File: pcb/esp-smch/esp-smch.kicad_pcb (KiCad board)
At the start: 2 copper layers, 54.7 x 41.5 mm, 7 parts, among them U1 WeMos_D1_mini, U2 NRF24L01_Breakout

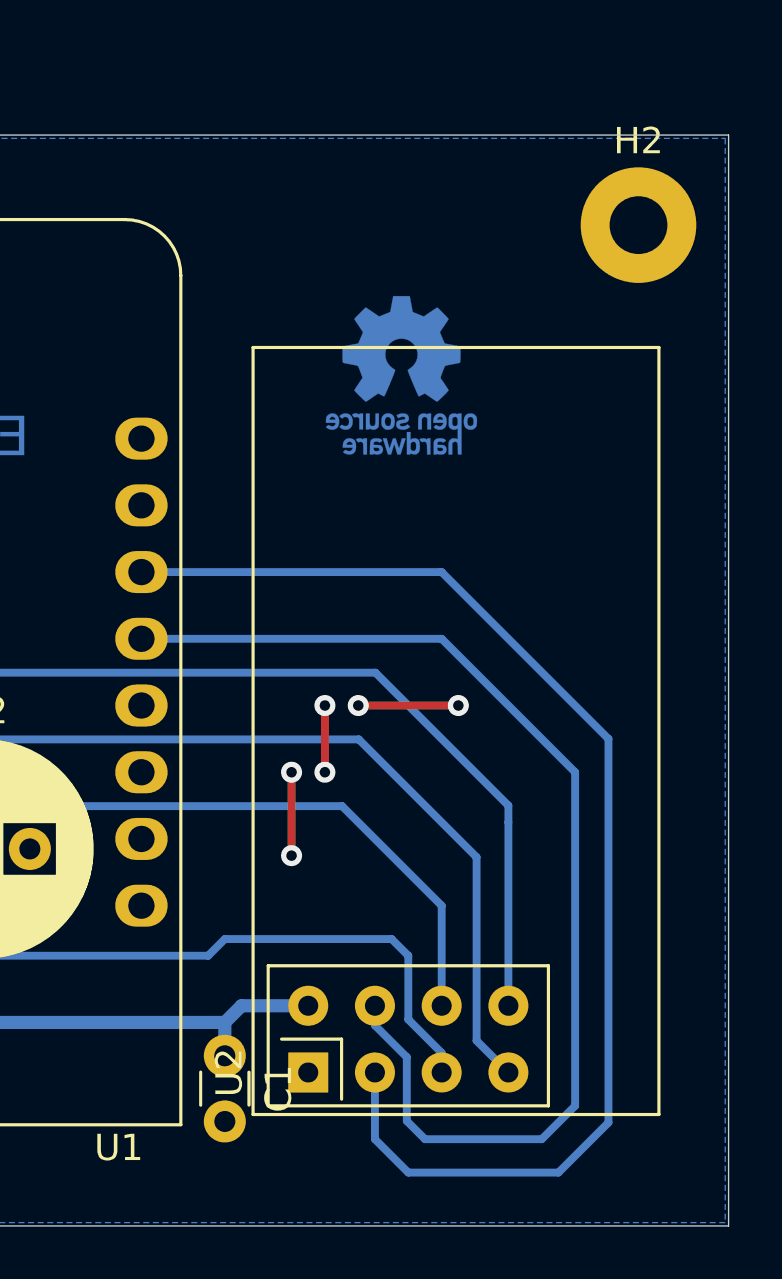
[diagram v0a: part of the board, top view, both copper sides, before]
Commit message: PCB: use nRF24L01+ PA-LNA breakout board
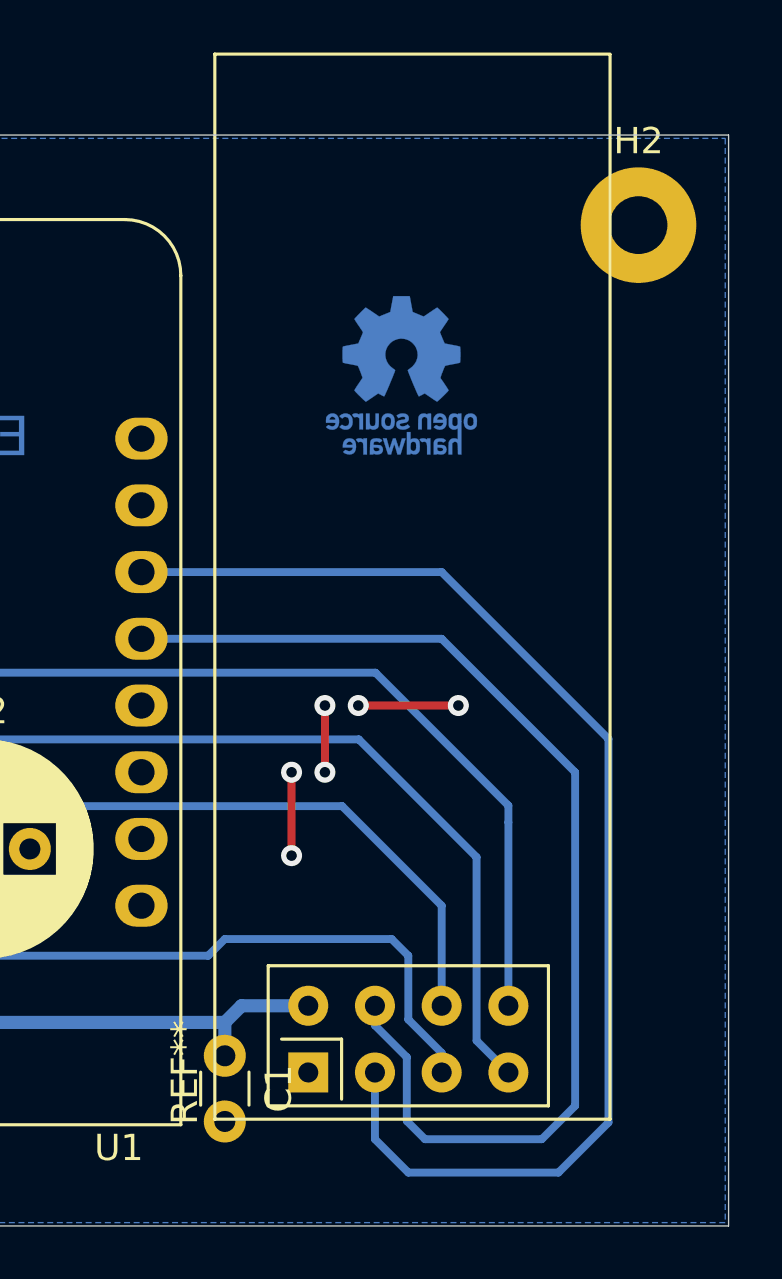
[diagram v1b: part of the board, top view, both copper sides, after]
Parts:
- U2: footprint RF_Module:nRF24L01_Breakout -> RF_Module:NRF24L01P_PA_LNA_Breakout
- moved U2 4.15 mm to (157.7, 112.1)
- renumbered LOGO to LOGO1

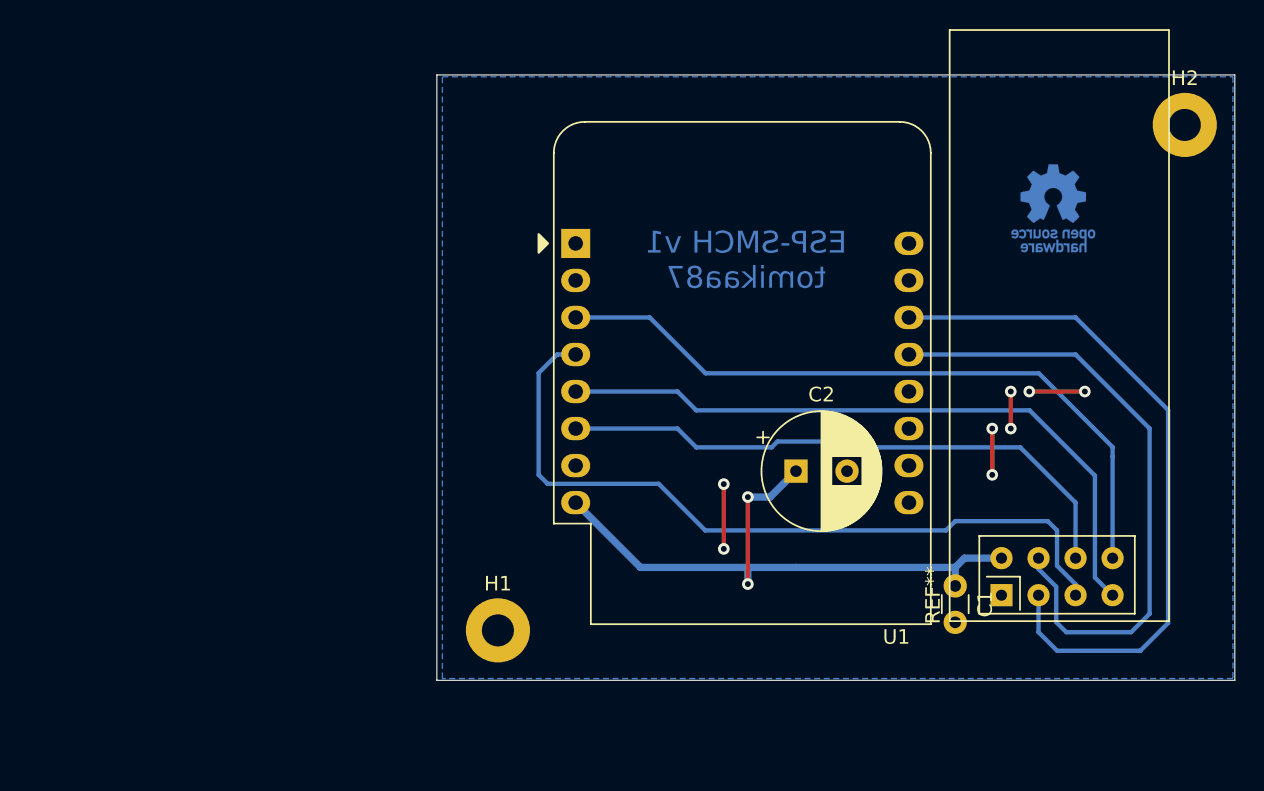
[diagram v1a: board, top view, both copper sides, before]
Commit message: PCB: new layout
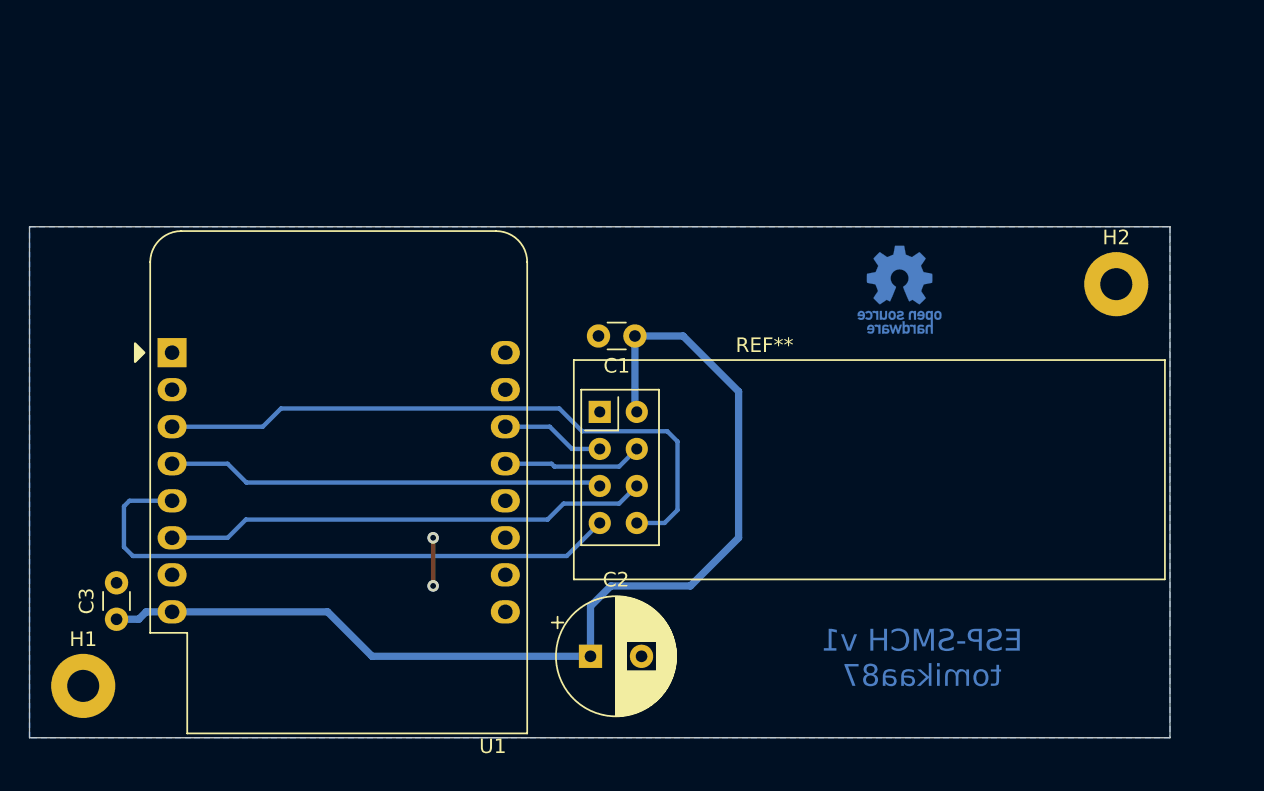
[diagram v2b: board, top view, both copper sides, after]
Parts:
- added C3: 100n, Capacitor_THT:C_Disc_D3.0mm_W1.6mm_P2.50mm, F.Cu at (100.7, 111.9)
- U2: footprint RF_Module:NRF24L01P_PA_LNA_Breakout -> esp-smch:NRF24L01P_PA_LNA_Breakout
- moved U2 31.5 mm to (132.0, 94.0), turned to 0 degrees
- moved H1 28.7 mm to (98.4, 116.5)
- moved U1 28.7 mm to (104.5, 93.6)
- moved C1 27.9 mm to (136.3, 92.5), turned to 180 degrees
- moved C2 19.0 mm to (133.2, 114.4)
- moved LOGO1 11.9 mm to (154.4, 89.3)
- moved H2 11.9 mm to (169.3, 88.9)
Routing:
- net Net-(U1-Pad14): track 47.8 -> 7.11 mm
- net Net-(U1-Pad13): track 43.4 -> 9.60 mm
- net +3V3: track 43.7 -> 73.5 mm, vias 2 -> 0
- net Net-(U1-Pad4): track 52.7 -> 30.0 mm
- net GND: track 14.0 -> 3.30 mm, vias 8 -> 2
- net Net-(U1-Pad6): track 40.5 -> 33.3 mm
- net Net-(U1-Pad5): track 46.7 -> 40.1 mm
- net Net-(U1-Pad3): track 48.1 -> 44.0 mm
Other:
- board size 54.7 x 41.5 mm -> 78.2 x 35.1 mm
- net class Power added: clearance 0.3, trace_width 0.5, via_dia 0.8, via_drill 0.4
